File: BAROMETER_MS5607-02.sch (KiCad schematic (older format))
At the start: 2 parts

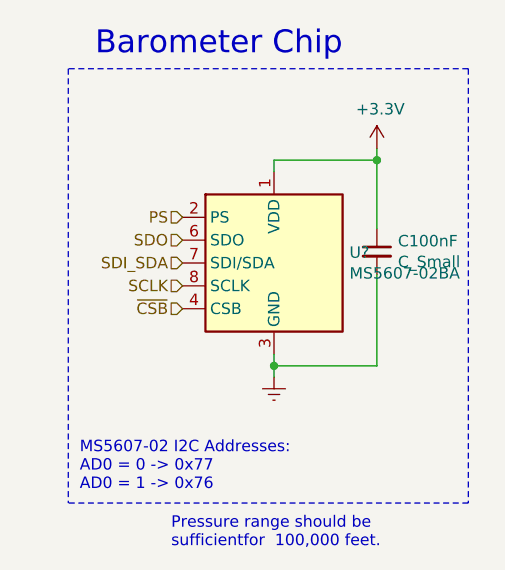
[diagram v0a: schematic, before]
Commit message: Edit to bus
Bus changed as well as some other things to almost finish it up
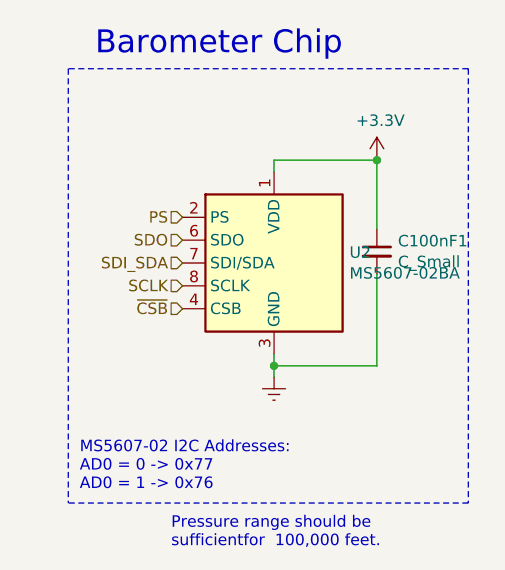
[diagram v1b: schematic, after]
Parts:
- gave numbers to parts that had none: 1
- renumbered C100nF to C100nF1
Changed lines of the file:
@@
 $Descr A4 11693 8268
 encoding utf-8
-Sheet 3 3
+Sheet 2 4
 Title "MS5607-02BA Barometer Chip"
 Date "2021-10-01"
@@
 	5900 3200 6350 3200
 Wire Wire Line
-	6350 3200 6350 3150
-Wire Wire Line
 	5900 4100 6350 4100
 Connection ~ 5900 4100
@@
 Text Notes 6200 2750 2    100  ~ 0
 Barometer Chip
-Connection ~ 6350 3200
 Wire Wire Line
 	6350 3200 6350 3500
@@
 Pressure range should be \nsufficientfor ~ 100,000 feet.
 $Comp
-L power:+3.3V #PWR?
-U 1 1 619A1EC3
-P 6350 3150
-F 0 "#PWR?" H 6350 3000 50  0001 C CNN
-F 1 "+3.3V" H 6365 3323 50  0000 C CNN
-F 2 "" H 6350 3150 50  0001 C CNN
-F 3 "" H 6350 3150 50  0001 C CNN
-	1    6350 3150
-	1    0    0    -1
-$EndComp
-$Comp
-L Sensor_Pressure:MS5607-02BA U?
+L Sensor_Pressure:MS5607-02BA U2
 U 1 1 619AA1D5
 P 5900 3650
-F 0 "U?" H 6230 3696 50  0000 L CNN
+F 0 "U2" H 6230 3696 50  0000 L CNN
 F 1 "MS5607-02BA" H 6230 3605 50  0000 L CNN
 F 2 "Package_LGA:LGA-8_3x5mm_P1.25mm" H 5900 3650 50  0001 C CNN
@@
 $EndComp
 $Comp
-L power:Earth #PWR?
+L power:Earth #PWR0136
 U 1 1 619ADA7B
 P 5900 4150
-F 0 "#PWR?" H 5900 3900 50  0001 C CNN
+F 0 "#PWR0136" H 5900 3900 50  0001 C CNN
 F 1 "Earth" H 5900 4000 50  0001 C CNN
 F 2 "" H 5900 4150 50  0001 C CNN
@@
 $EndComp
 $Comp
-L Device:C_Small C100nF
+L Device:C_Small C100nF1
 U 1 1 619AE3A1
 P 6350 3600
-F 0 "C100nF" H 6442 3646 50  0000 L CNN
+F 0 "C100nF1" H 6442 3646 50  0000 L CNN
 F 1 "C_Small" H 6442 3555 50  0000 L CNN
 F 2 "" H 6350 3600 50  0001 C CNN
@@
 Text HLabel 5500 3450 0    50   Input ~ 0
 PS
+$Comp
+L power:+3.3V #PWR0101
+U 1 1 61A7CC2D
+P 6350 3200
+F 0 "#PWR0101" H 6350 3050 50  0001 C CNN
+F 1 "+3.3V" H 6365 3373 50  0000 C CNN
+F 2 "" H 6350 3200 50  0001 C CNN
+F 3 "" H 6350 3200 50  0001 C CNN
+	1    6350 3200
+	1    0    0    -1
+$EndComp
+Connection ~ 6350 3200
 $EndSCHEMATC

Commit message: Updated PCB
Finalized most of the charges board and PCB
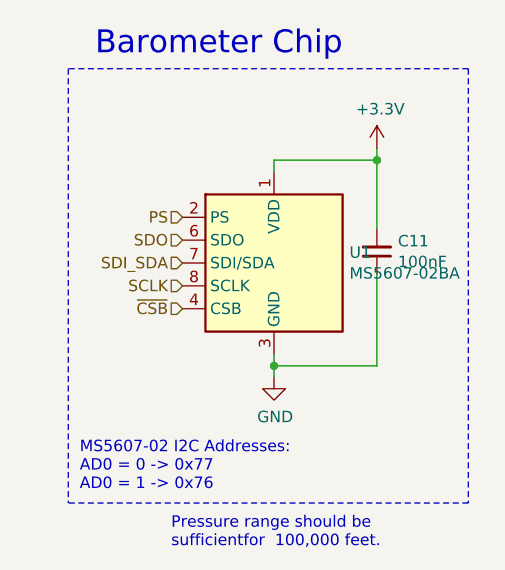
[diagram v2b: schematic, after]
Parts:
- removed C100nF1: C_Small, symbol Device:C_Small
- added C11: 100nF, Capacitor_SMD:C_0603_1608Metric, symbol Device:C_Small
- renumbered U2 to U1
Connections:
- net +3V3: now also C11.2
- net Earth renamed GND
- net GND: now also C11.1
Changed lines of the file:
@@
 $Descr A4 11693 8268
 encoding utf-8
-Sheet 2 4
+Sheet 3 4
 Title "MS5607-02BA Barometer Chip"
 Date "2021-10-01"
@@
 Comment4 ""
 $EndDescr
-Wire Wire Line
-	5900 3200 5900 3250
-Wire Wire Line
-	5900 4050 5900 4100
-Wire Wire Line
-	5900 3200 6350 3200
-Wire Wire Line
-	5900 4100 6350 4100
-Connection ~ 5900 4100
-Wire Wire Line
-	5900 4100 5900 4150
 Wire Notes Line
 	6750 2800 5000 2800
 Text Notes 6200 2750 2    100  ~ 0
 Barometer Chip
-Wire Wire Line
-	6350 3200 6350 3500
 Text HLabel 5500 3650 0    50   Input ~ 0
 SDI_SDA
@@
 Text Notes 5450 4900 0    50   ~ 0
 Pressure range should be \nsufficientfor ~ 100,000 feet.
+Wire Wire Line
+	6350 3700 6350 4100
+Text HLabel 5500 3450 0    50   Input ~ 0
+PS
 $Comp
-L Sensor_Pressure:MS5607-02BA U2
+L Sensor_Pressure:MS5607-02BA U1
 U 1 1 619AA1D5
 P 5900 3650
-F 0 "U2" H 6230 3696 50  0000 L CNN
+F 0 "U1" H 6230 3696 50  0000 L CNN
 F 1 "MS5607-02BA" H 6230 3605 50  0000 L CNN
 F 2 "Package_LGA:LGA-8_3x5mm_P1.25mm" H 5900 3650 50  0001 C CNN
@@
 	1    0    0    -1
 $EndComp
+Wire Wire Line
+	6350 3150 6350 3200
+Wire Wire Line
+	5900 3250 5900 3200
+Wire Wire Line
+	5900 3200 6350 3200
+Connection ~ 6350 3200
 $Comp
-L power:Earth #PWR0136
-U 1 1 619ADA7B
+L power:+3.3V #PWR0103
+U 1 1 61AE4A67
+P 6350 3150
+F 0 "#PWR0103" H 6350 3000 50  0001 C CNN
+F 1 "+3.3V" H 6365 3323 50  0000 C CNN
+F 2 "" H 6350 3150 50  0001 C CNN
+F 3 "" H 6350 3150 50  0001 C CNN
+	1    6350 3150
+	1    0    0    -1
+$EndComp
+Wire Wire Line
+	5900 4050 5900 4100
+Wire Wire Line
+	5900 4100 6350 4100
+Connection ~ 5900 4100
+Wire Wire Line
+	5900 4100 5900 4150
+Wire Wire Line
+	6350 3200 6350 3500
+$Comp
+L Device:C_Small C?
+U 1 1 61B849BE
+P 6350 3600
+AR Path="/61B849BE" Ref="C?"  Part="1"
+AR Path="/6160DF75/61B849BE" Ref="C?"  Part="1"
+AR Path="/6199791F/61B849BE" Ref="C11"  Part="1"
+F 0 "C11" H 6258 3554 50  0000 R CNN
+F 1 "100nF" H 6258 3645 50  0000 R CNN
+F 2 "Capacitor_SMD:C_0603_1608Metric" H 6350 3600 50  0001 C CNN
+F 3 "~" H 6350 3600 50  0001 C CNN
+	1    6350 3600
+	-1   0    0    1
+$EndComp
+$Comp
+L power:GND #PWR0113
+U 1 1 61C97D78
 P 5900 4150
-F 0 "#PWR0136" H 5900 3900 50  0001 C CNN
-F 1 "Earth" H 5900 4000 50  0001 C CNN
+F 0 "#PWR0113" H 5900 3900 50  0001 C CNN
+F 1 "GND" H 5905 3977 50  0000 C CNN
 F 2 "" H 5900 4150 50  0001 C CNN
-F 3 "~" H 5900 4150 50  0001 C CNN
+F 3 "" H 5900 4150 50  0001 C CNN
 	1    5900 4150
 	1    0    0    -1
 $EndComp
-$Comp
-L Device:C_Small C100nF1
-U 1 1 619AE3A1
-P 6350 3600
-F 0 "C100nF1" H 6442 3646 50  0000 L CNN
-F 1 "C_Small" H 6442 3555 50  0000 L CNN
-F 2 "" H 6350 3600 50  0001 C CNN
-F 3 "~" H 6350 3600 50  0001 C CNN
-	1    6350 3600
-	1    0    0    -1
-$EndComp
-Wire Wire Line
-	6350 3700 6350 4100
-Text HLabel 5500 3450 0    50   Input ~ 0
-PS
-$Comp
-L power:+3.3V #PWR0101
-U 1 1 61A7CC2D
-P 6350 3200
-F 0 "#PWR0101" H 6350 3050 50  0001 C CNN
-F 1 "+3.3V" H 6365 3373 50  0000 C CNN
-F 2 "" H 6350 3200 50  0001 C CNN
-F 3 "" H 6350 3200 50  0001 C CNN
-	1    6350 3200
-	1    0    0    -1
-$EndComp
-Connection ~ 6350 3200
 $EndSCHEMATC

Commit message: Fix to components
Changed the buzzer and terminal blocks
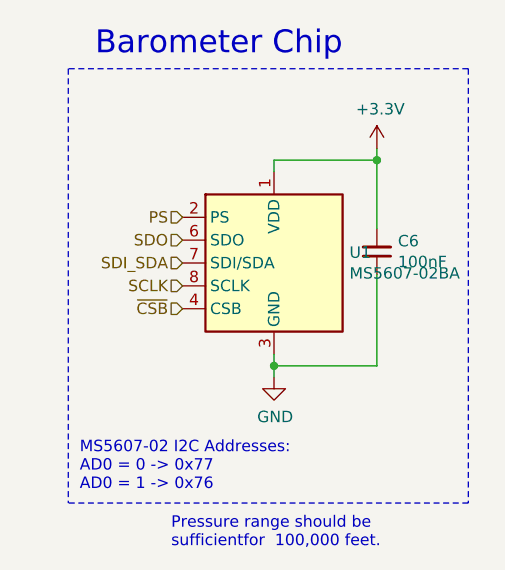
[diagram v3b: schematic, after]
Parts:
- renumbered C11 to C6
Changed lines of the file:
@@
 Connection ~ 6350 3200
 $Comp
-L power:+3.3V #PWR0103
+L power:+3.3V #PWR031
 U 1 1 61AE4A67
 P 6350 3150
-F 0 "#PWR0103" H 6350 3000 50  0001 C CNN
+F 0 "#PWR031" H 6350 3000 50  0001 C CNN
 F 1 "+3.3V" H 6365 3323 50  0000 C CNN
 F 2 "" H 6350 3150 50  0001 C CNN
@@
 AR Path="/61B849BE" Ref="C?"  Part="1"
 AR Path="/6160DF75/61B849BE" Ref="C?"  Part="1"
-AR Path="/6199791F/61B849BE" Ref="C11"  Part="1"
-F 0 "C11" H 6258 3554 50  0000 R CNN
+AR Path="/6199791F/61B849BE" Ref="C6"  Part="1"
+F 0 "C6" H 6258 3554 50  0000 R CNN
 F 1 "100nF" H 6258 3645 50  0000 R CNN
 F 2 "Capacitor_SMD:C_0603_1608Metric" H 6350 3600 50  0001 C CNN
@@
 $EndComp
 $Comp
-L power:GND #PWR0113
+L power:GND #PWR030
 U 1 1 61C97D78
 P 5900 4150
-F 0 "#PWR0113" H 5900 3900 50  0001 C CNN
+F 0 "#PWR030" H 5900 3900 50  0001 C CNN
 F 1 "GND" H 5905 3977 50  0000 C CNN
 F 2 "" H 5900 4150 50  0001 C CNN
